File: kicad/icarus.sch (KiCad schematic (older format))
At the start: 78 parts, among them J1 CAN Bus, J2 CAN Bus, J3 SWD Programming, J4 USB_B_Micro, Q1 BSS123, U1 MAX15062A, U10 XT30, U11 XT30, U12 XT30, U13 XT30, U14 LT1787HVIMS8PBF, U15 USBLC6-2SC6, U16 STLM20DD9FUDFN-4L_STM-L, U2 STM32G474CEU6, U3 TCAN334G, U4 ZXMP10A13FTA, U5 XT90, U6 FSV10150VTO277-3L_ONS-L, U7 XT30, U8 XT30, U9 TPS2490DGSR

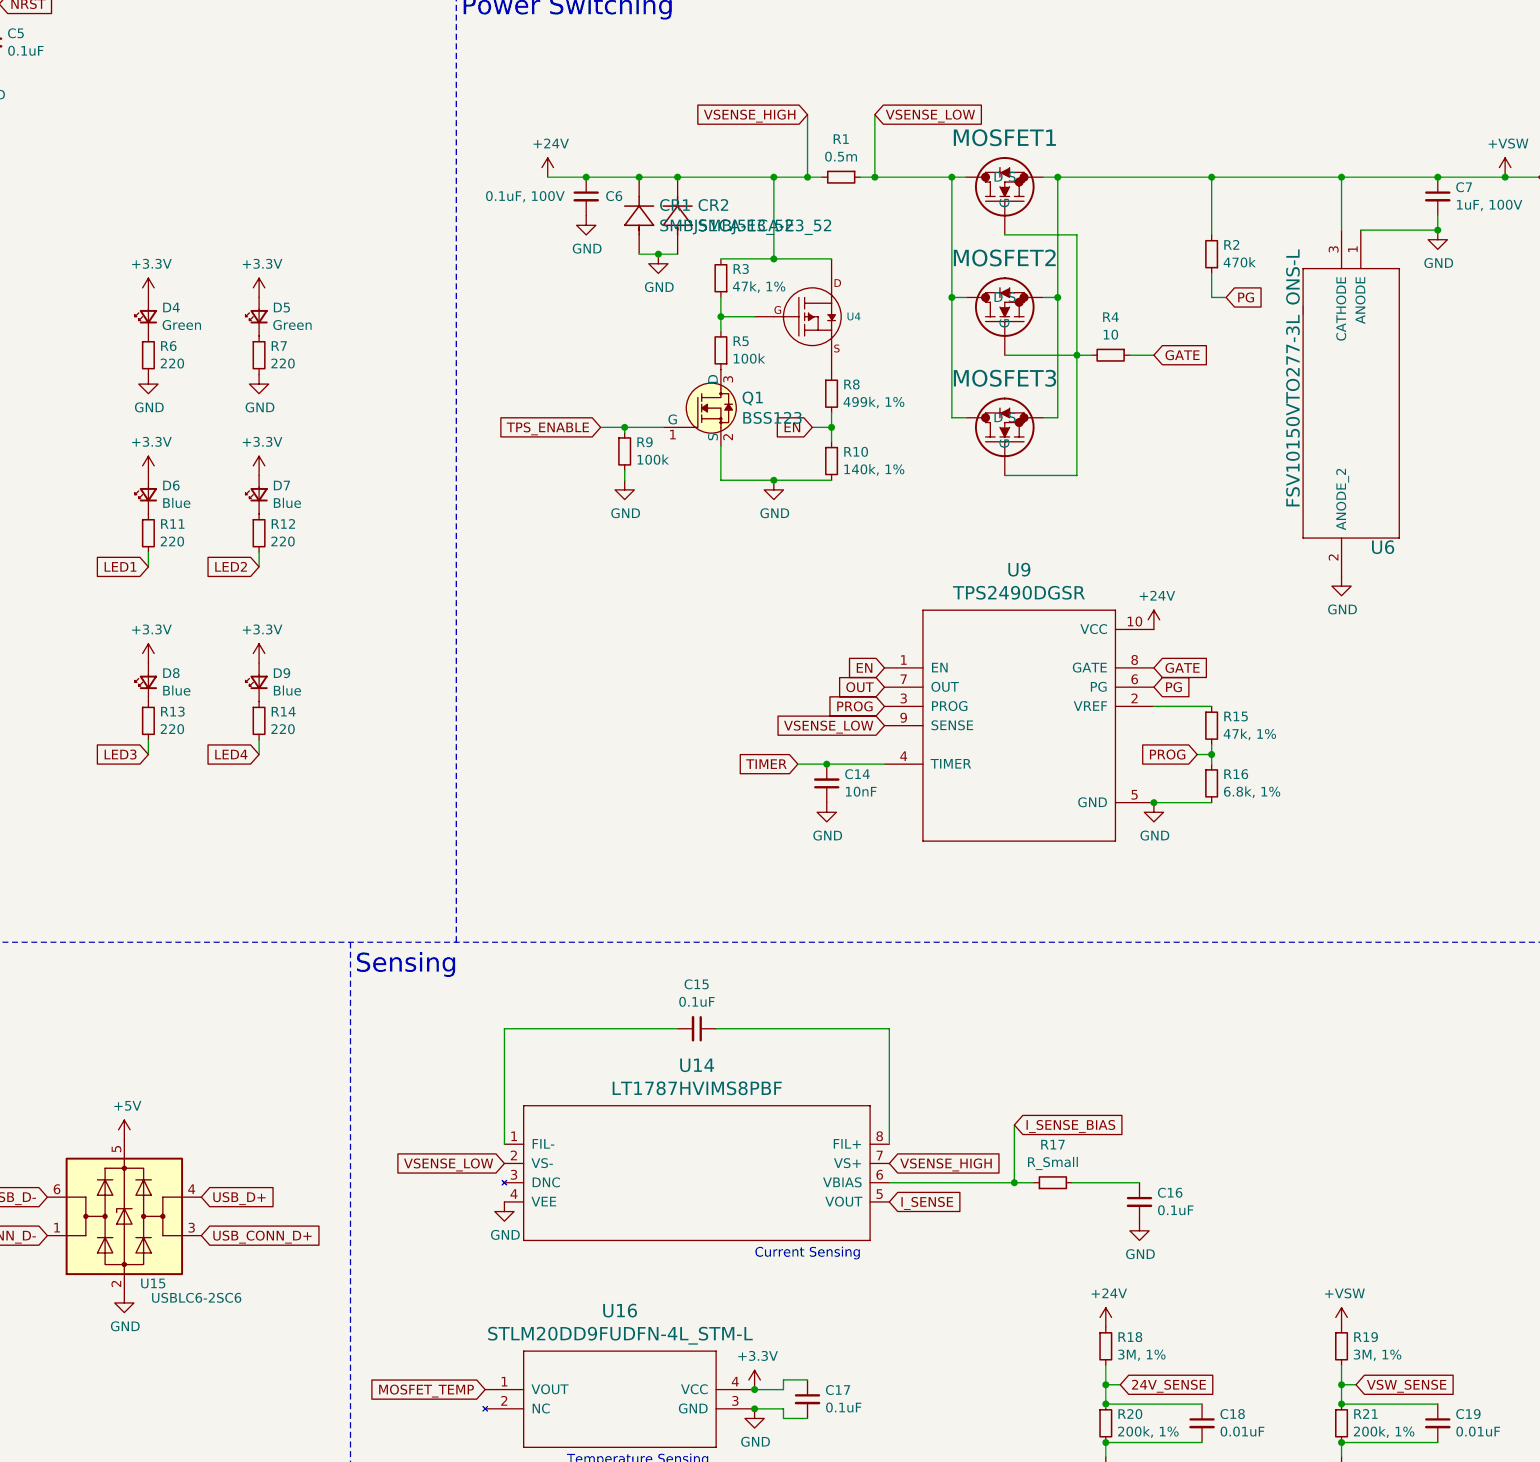
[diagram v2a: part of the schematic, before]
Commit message: Finished importing and modifying footprints
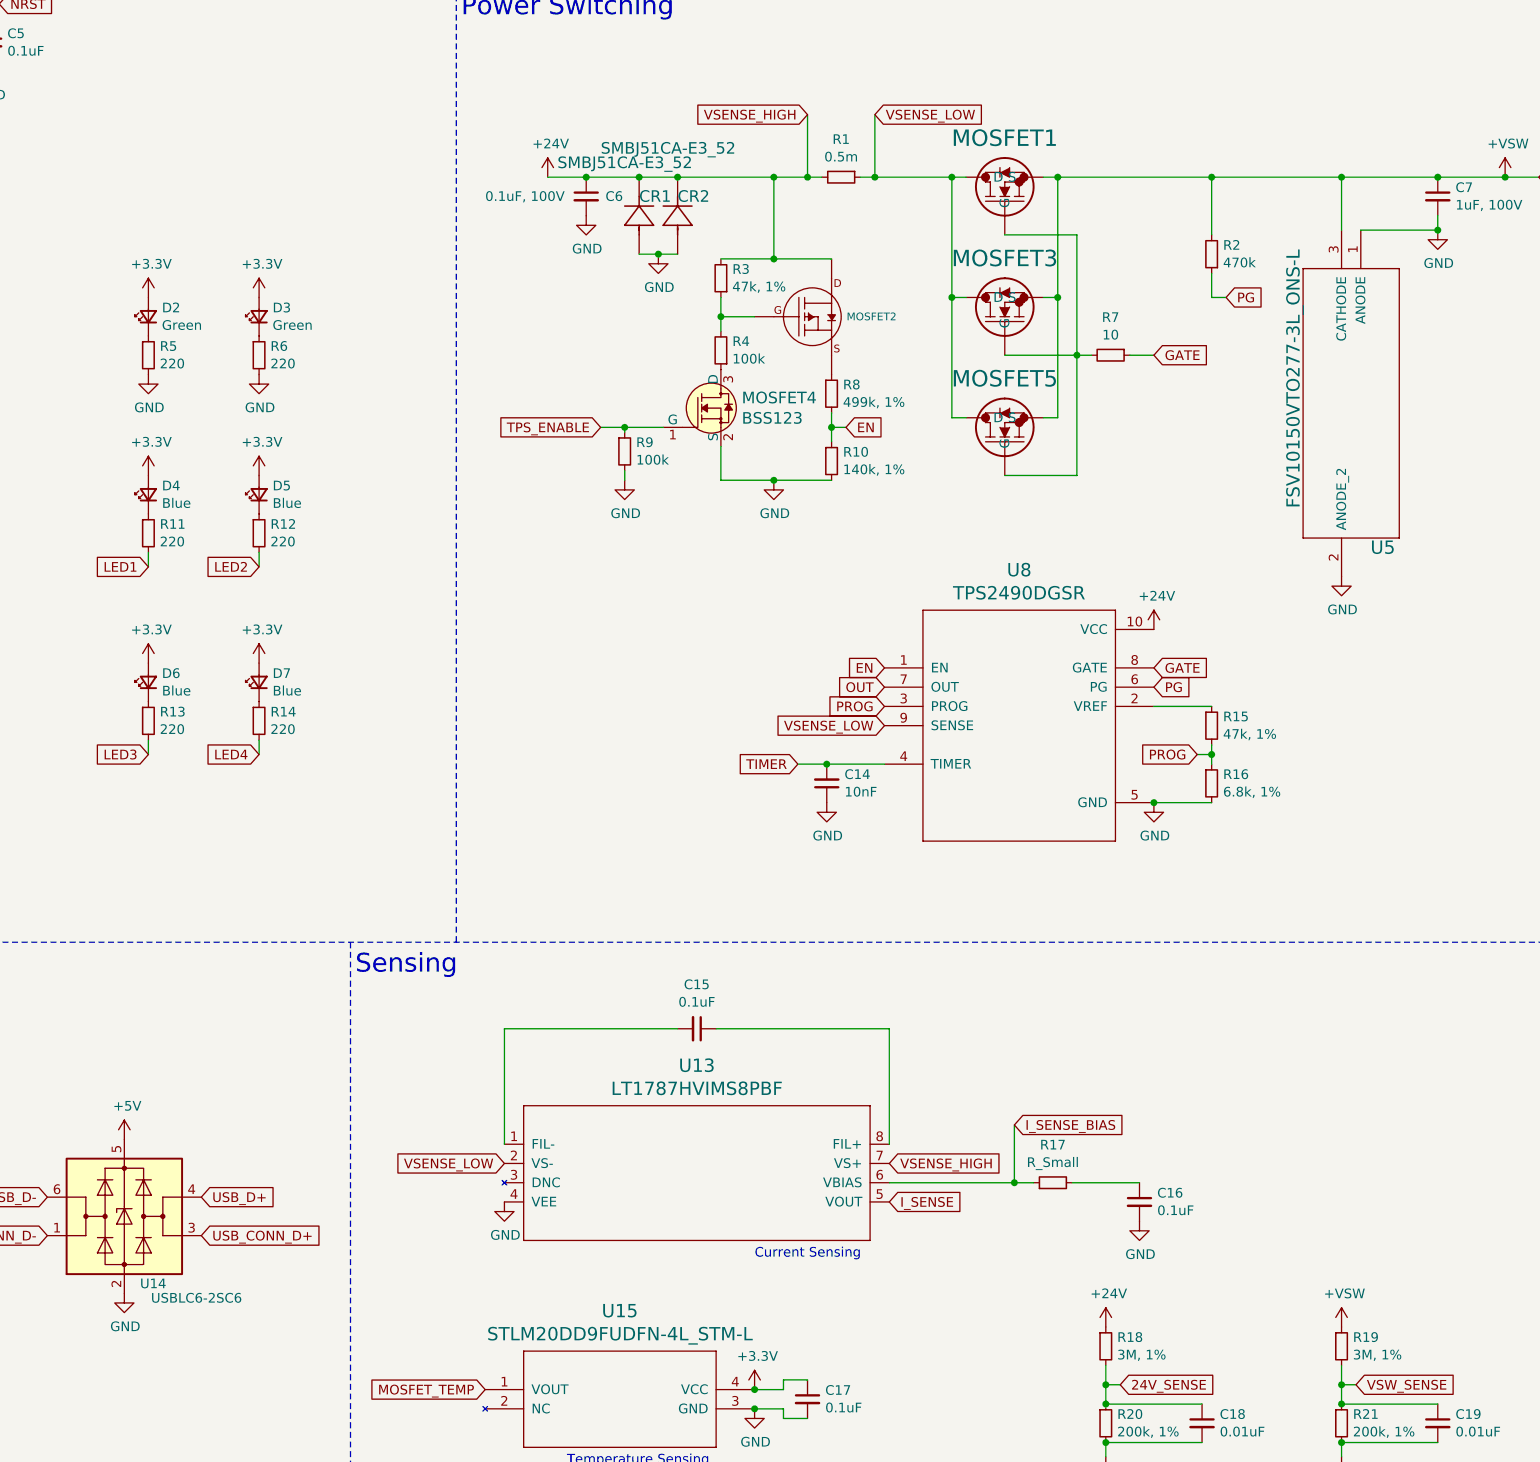
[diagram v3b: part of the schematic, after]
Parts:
- MOSFET2: renamed from U4; footprint digikey-footprints:SOT-23-3 -> icarus_kicad_lib:ZXMP10A13FTA
- renumbered D4 to D2, D5 to D3, D6 to D4, D7 to D5, D8 to D6, D9 to D7, MOSFET2 to MOSFET3, Q1 to MOSFET4, MOSFET3 to MOSFET5, R5 to R4, R6 to R5, R7 to R6, R4 to R7, U11 to U10, U12 to U11, U13 to U12, U14 to U13, U15 to U14, U16 to U15, U5 to U4, U6 to U5, U7 to U6, U8 to U7, U9 to U8, U10 to U9
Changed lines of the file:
@@
 $EndComp
 $Comp
-L Power_Protection:USBLC6-2SC6 U15
+L Power_Protection:USBLC6-2SC6 U14
 U 1 1 60480FBC
 P 4800 8925
-F 0 "U15" H 4950 8575 50  0000 C CNN
+F 0 "U14" H 4950 8575 50  0000 C CNN
 F 1 "USBLC6-2SC6" H 5175 8500 50  0000 C CNN
 F 2 "digikey-footprints:SOT-23-6" H 4800 8425 50  0001 C CNN
@@
 	13175 6475 13175 6600
 $Comp
-L xt30:XT30 U7
+L xt30:XT30 U6
 U 1 1 604E38EC
 P 15275 5700
-F 0 "U7" H 15325 5750 50  0001 C CNN
+F 0 "U6" H 15325 5750 50  0001 C CNN
 F 1 "XT30" H 15275 5700 50  0001 C CNN
 F 2 "icarus_kicad_lib:XT30P" H 15275 5700 50  0001 C CNN
@@
 $EndComp
 $Comp
-L xt30:XT30 U8
+L xt30:XT30 U7
 U 1 1 604E3CF6
 P 15275 6250
-F 0 "U8" H 15325 6300 50  0001 C CNN
+F 0 "U7" H 15325 6300 50  0001 C CNN
 F 1 "XT30" H 15275 6250 50  0001 C CNN
 F 2 "icarus_kicad_lib:XT30P" H 15275 6250 50  0001 C CNN
@@
 $EndComp
 $Comp
-L xt30:XT30 U10
+L xt30:XT30 U9
 U 1 1 604E3E54
 P 15275 6800
-F 0 "U10" H 15325 6850 50  0001 C CNN
+F 0 "U9" H 15325 6850 50  0001 C CNN
 F 1 "XT30" H 15275 6800 50  0001 C CNN
 F 2 "icarus_kicad_lib:XT30P" H 15275 6800 50  0001 C CNN
@@
 $EndComp
 $Comp
-L xt30:XT30 U11
+L xt30:XT30 U10
 U 1 1 604E4ABF
 P 15275 7350
-F 0 "U11" H 15325 7400 50  0001 C CNN
+F 0 "U10" H 15325 7400 50  0001 C CNN
 F 1 "XT30" H 15275 7350 50  0001 C CNN
 F 2 "icarus_kicad_lib:XT30P" H 15275 7350 50  0001 C CNN
@@
 $EndComp
 $Comp
-L xt30:XT30 U12
+L xt30:XT30 U11
 U 1 1 604E507D
 P 15275 7900
-F 0 "U12" H 15325 7950 50  0001 C CNN
+F 0 "U11" H 15325 7950 50  0001 C CNN
 F 1 "XT30" H 15275 7900 50  0001 C CNN
 F 2 "icarus_kicad_lib:XT30P" H 15275 7900 50  0001 C CNN
@@
 $EndComp
 $Comp
-L xt30:XT30 U13
+L xt30:XT30 U12
 U 1 1 604E565A
 P 15275 8450
-F 0 "U13" H 15325 8500 50  0001 C CNN
+F 0 "U12" H 15325 8500 50  0001 C CNN
 F 1 "XT30" H 15275 8450 50  0001 C CNN
 F 2 "icarus_kicad_lib:XT30P" H 15275 8450 50  0001 C CNN
@@
 ICARUS
 $Comp
-L tps2490dgsr:TPS2490DGSR U9
+L tps2490dgsr:TPS2490DGSR U8
 U 1 1 60502360
 P 9450 6375
-F 0 "U9" H 9450 7183 69  0000 C CNN
+F 0 "U8" H 9450 7183 69  0000 C CNN
 F 1 "TPS2490DGSR" H 9450 7063 69  0000 C CNN
 F 2 "icarus_kicad_lib:TPS2490DGSR" H 9450 6375 50  0001 C CNN
@@
 $EndComp
 $Comp
-L Device:LED_Small D5
+L Device:LED_Small D3
 U 1 1 607A30EE
 P 5500 4250
-F 0 "D5" V 5546 4180 50  0000 R CNN
+F 0 "D3" V 5546 4180 50  0000 R CNN
 F 1 "Green" V 5455 4180 50  0000 R CNN
 F 2 "LED_SMD:LED_0603_1608Metric" V 5500 4250 50  0001 C CNN
@@
 $EndComp
 $Comp
-L Device:R_Small R7
+L Device:R_Small R6
 U 1 1 607A30F4
 P 5500 4450
-F 0 "R7" H 5559 4496 50  0000 L CNN
+F 0 "R6" H 5559 4496 50  0000 L CNN
 F 1 "220" H 5559 4405 50  0000 L CNN
 F 2 "Resistor_SMD:R_0402_1005Metric" H 5500 4450 50  0001 C CNN
@@
 $EndComp
 $Comp
-L Device:LED_Small D6
+L Device:LED_Small D4
 U 1 1 607B09D4
 P 4925 5175
-F 0 "D6" V 4971 5105 50  0000 R CNN
+F 0 "D4" V 4971 5105 50  0000 R CNN
 F 1 "Blue" V 4880 5105 50  0000 R CNN
 F 2 "LED_SMD:LED_0603_1608Metric" V 4925 5175 50  0001 C CNN
@@
 $EndComp
 $Comp
-L Device:LED_Small D4
+L Device:LED_Small D2
 U 1 1 607D3F96
 P 4925 4250
-F 0 "D4" V 4971 4180 50  0000 R CNN
+F 0 "D2" V 4971 4180 50  0000 R CNN
 F 1 "Green" V 4880 4180 50  0000 R CNN
 F 2 "LED_SMD:LED_0603_1608Metric" V 4925 4250 50  0001 C CNN
@@
 $EndComp
 $Comp
-L Device:R_Small R6
+L Device:R_Small R5
 U 1 1 607D3F9C
 P 4925 4450
-F 0 "R6" H 4984 4496 50  0000 L CNN
+F 0 "R5" H 4984 4496 50  0000 L CNN
 F 1 "220" H 4984 4405 50  0000 L CNN
 F 2 "Resistor_SMD:R_0402_1005Metric" H 4925 4450 50  0001 C CNN
@@
 $EndComp
 $Comp
-L Device:LED_Small D7
+L Device:LED_Small D5
 U 1 1 607DF041
 P 5500 5175
-F 0 "D7" V 5546 5105 50  0000 R CNN
+F 0 "D5" V 5546 5105 50  0000 R CNN
 F 1 "Blue" V 5455 5105 50  0000 R CNN
 F 2 "LED_SMD:LED_0603_1608Metric" V 5500 5175 50  0001 C CNN
@@
 Connection ~ 1250 5525
 $Comp
-L lt1787hvims8pbf:LT1787HVIMS8PBF U14
+L lt1787hvims8pbf:LT1787HVIMS8PBF U13
 U 1 1 608530FA
 P 6575 8550
-F 0 "U14" H 7775 8958 69  0000 C CNN
+F 0 "U13" H 7775 8958 69  0000 C CNN
 F 1 "LT1787HVIMS8PBF" H 7775 8838 69  0000 C CNN
 F 2 "icarus_kicad_lib:LT1787HVIMS8PBF" H 6575 8550 50  0001 C CNN
@@
 $EndComp
 $Comp
-L xt30:XT30 U5
+L xt30:XT30 U4
 U 1 1 60883C89
 P 15275 4775
-F 0 "U5" H 15325 4825 50  0001 C CNN
+F 0 "U4" H 15325 4825 50  0001 C CNN
 F 1 "XT90" H 15275 4775 50  0001 C CNN
 F 2 "icarus_kicad_lib:XT90PW-M" H 15275 4775 50  0001 C CNN
@@
 Current Sensing
 $Comp
-L stlm20dd9fudfn-4l_stm-l:STLM20DD9FUDFN-4L_STM-L U16
+L stlm20dd9fudfn-4l_stm-l:STLM20DD9FUDFN-4L_STM-L U15
 U 1 1 60896628
 P 6575 9825
-F 0 "U16" H 7375 10233 69  0000 C CNN
+F 0 "U15" H 7375 10233 69  0000 C CNN
 F 1 "STLM20DD9FUDFN-4L_STM-L" H 7375 10113 69  0000 C CNN
 F 2 "icarus_kicad_lib:STLM20DD9FUDFN-4L_STM-L" H 6575 9825 50  0001 C CNN
@@
 	11625 3525 11975 3525
 $Comp
-L fsv10150vto277-3l_ons-l:FSV10150VTO277-3L_ONS-L U6
+L fsv10150vto277-3l_ons-l:FSV10150VTO277-3L_ONS-L U5
 U 1 1 60A04254
 P 11125 5700
-F 0 "U6" V 11375 5550 69  0000 R CNN
+F 0 "U5" V 11375 5550 69  0000 R CNN
 F 1 "FSV10150VTO277-3L_ONS-L" H 12925 5950 69  0000 R CNN
 F 2 "icarus_kicad_lib:FSV10150VTO277-3L_ONS-L" H 11125 5700 50  0001 C CNN
@@
 	1    0    0    -1
 $EndComp
-Text GLabel 8375 4825 0    50   Input ~ 0
+Text GLabel 8550 4825 2    50   Input ~ 0
 EN
-Wire Wire Line
-	8375 4825 8475 4825
-Wire Wire Line
-	8475 4750 8475 4825
-Connection ~ 8475 4825
-Wire Wire Line
-	8475 4825 8475 4900
 Text GLabel 8700 3200 2    50   Input ~ 0
 VSENSE_LOW
@@
 GATE
 $Comp
-L Device:R_Small R4
+L Device:R_Small R7
 U 1 1 605F126E
 P 9925 4450
-F 0 "R4" V 9729 4450 50  0000 C CNN
+F 0 "R7" V 9729 4450 50  0000 C CNN
 F 1 "10" V 9820 4450 50  0000 C CNN
 F 2 "Resistor_SMD:R_0402_1005Metric" H 9925 4450 50  0001 C CNN
@@
 $EndComp
 $Comp
-L p-channel_fet_sot-23-3:P-CHANNEL_FET_SOT-23-3 U4
+L p-channel_fet_sot-23-3:P-CHANNEL_FET_SOT-23-3 MOSFET2
 U 1 1 60BF3EC6
 P 8375 4250
-F 0 "U4" H 8553 4250 40  0000 L CNN
+F 0 "MOSFET2" H 8553 4250 40  0000 L CNN
 F 1 "ZXMP10A13FTA" H 8553 4212 40  0001 L CNN
-F 2 "digikey-footprints:SOT-23-3" H 8375 4250 50  0001 C CNN
+F 2 "icarus_kicad_lib:ZXMP10A13FTA" H 8375 4250 50  0001 C CNN
 F 3 "" H 8375 4250 50  0001 C CNN
 	1    8375 4250
@@
 $EndComp
 $Comp
-L Device:R_Small R5
+L Device:R_Small R4
 U 1 1 60BF6AD0
 P 7900 4425
-F 0 "R5" H 7841 4379 50  0000 R CNN
+F 0 "R4" H 7841 4379 50  0000 R CNN
 F 1 "100k" H 7841 4470 50  0000 R CNN
 F 2 "Resistor_SMD:R_0402_1005Metric" H 7900 4425 50  0001 C CNN
@@
 Connection ~ 3225 6750
 $Comp
-L Device:LED_Small D8
+L Device:LED_Small D6
 U 1 1 604C7C67
 P 4925 6150
-F 0 "D8" V 4971 6080 50  0000 R CNN
+F 0 "D6" V 4971 6080 50  0000 R CNN
 F 1 "Blue" V 4880 6080 50  0000 R CNN
 F 2 "LED_SMD:LED_0603_1608Metric" V 4925 6150 50  0001 C CNN
@@
 LED3
 $Comp
-L Device:LED_Small D9
+L Device:LED_Small D7
 U 1 1 604C7C7B
 P 5500 6150
-F 0 "D9" V 5546 6080 50  0000 R CNN
+F 0 "D7" V 5546 6080 50  0000 R CNN
 F 1 "Blue" V 5455 6080 50  0000 R CNN
 F 2 "LED_SMD:LED_0603_1608Metric" V 5500 6150 50  0001 C CNN
@@
 $EndComp
 $Comp
-L icarus-rescue:PSMN4R8-100BSEJ-psmn4r8-100bsej MOSFET2
+L icarus-rescue:PSMN4R8-100BSEJ-psmn4r8-100bsej MOSFET3
 U 1 1 6088724D
 P 9375 4450
-F 0 "MOSFET2" V 9877 4450 85  0000 C CNN
+F 0 "MOSFET3" V 9877 4450 85  0000 C CNN
 F 1 "PSMN4R8-100BSEJ" V 9877 4450 85  0001 C CNN
 F 2 "icarus_kicad_lib:PSMN4R8-100BSEJ" H 9375 4450 50  0001 C CNN
@@
 $EndComp
 $Comp
-L icarus-rescue:PSMN4R8-100BSEJ-psmn4r8-100bsej MOSFET3
+L icarus-rescue:PSMN4R8-100BSEJ-psmn4r8-100bsej MOSFET5
 U 1 1 60888AB1
 P 9375 5075
-F 0 "MOSFET3" V 9877 5075 85  0000 C CNN
+F 0 "MOSFET5" V 9877 5075 85  0000 C CNN
 F 1 "PSMN4R8-100BSEJ" V 9877 5075 85  0001 C CNN
 F 2 "icarus_kicad_lib:PSMN4R8-100BSEJ" H 9375 5075 50  0001 C CNN
@@
 U 1 1 608E4AFE
 P 7475 3925
-F 0 "CR1" V 7728 3821 60  0000 R CNN
-F 1 "SMBJ51CA-E3_52" V 7622 3821 60  0000 R CNN
+F 0 "CR1" V 7775 3925 60  0000 R CNN
+F 1 "SMBJ51CA-E3_52" V 7950 4350 60  0000 R CNN
 F 2 "icarus_kicad_lib:SMBJ51CA-E3-52" H 7675 3565 60  0001 C CNN
 F 3 "" H 7475 3925 60  0000 C CNN
@@
 U 1 1 608F0D36
 P 7675 3925
-F 0 "CR2" V 7928 3821 60  0000 R CNN
-F 1 "SMBJ51CA-E3_52" V 7822 3821 60  0000 R CNN
+F 0 "CR2" V 7975 3925 60  0000 R CNN
+F 1 "SMBJ51CA-E3_52" V 8225 4325 60  0000 R CNN
 F 2 "icarus_kicad_lib:SMBJ51CA-E3-52" H 7875 3565 60  0001 C CNN
 F 3 "" H 7675 3925 60  0000 C CNN
@@
 	7575 3925 7675 3925
 $Comp
-L dk_Transistors-FETs-MOSFETs-Single:BSS123 Q1
+L dk_Transistors-FETs-MOSFETs-Single:BSS123 MOSFET4
 U 1 1 60925E78
 P 7900 4725
-F 0 "Q1" H 8008 4778 60  0000 L CNN
+F 0 "MOSFET4" H 8008 4778 60  0000 L CNN
 F 1 "BSS123" H 8008 4672 60  0000 L CNN
 F 2 "digikey-footprints:SOT-23-3" H 8100 4925 60  0001 L CNN
@@
 	0    1    1    0
 $EndComp
+Wire Wire Line
+	8475 4750 8475 4825
+Wire Wire Line
+	8550 4825 8475 4825
+Connection ~ 8475 4825
+Wire Wire Line
+	8475 4825 8475 4900
 $EndSCHEMATC

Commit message: Initial rough layout done
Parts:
- J1, J2: footprint Connector_JST:JST_PH_B3B-PH-SM4-TB_1x03-1MP_P2.00mm_Vertical -> Connector_JST:JST_PH_B3B-PH-K_1x03_P2.00mm_Vertical
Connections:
- net GND: now also C10.2, C11.2, C12.2, C13.2, C8.2, C9.2
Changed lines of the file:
@@
 F 0 "J1" H 14055 3342 50  0000 L CNN
 F 1 "CAN Bus" H 14055 3251 50  0000 L CNN
-F 2 "Connector_JST:JST_PH_B3B-PH-SM4-TB_1x03-1MP_P2.00mm_Vertical" H 13975 3300 50  0001 C CNN
+F 2 "Connector_JST:JST_PH_B3B-PH-K_1x03_P2.00mm_Vertical" H 13975 3300 50  0001 C CNN
 F 3 "~" H 13975 3300 50  0001 C CNN
 	1    13975 3300
@@
 F 0 "J2" H 15230 3342 50  0000 L CNN
 F 1 "CAN Bus" H 15230 3251 50  0000 L CNN
-F 2 "Connector_JST:JST_PH_B3B-PH-SM4-TB_1x03-1MP_P2.00mm_Vertical" H 15150 3300 50  0001 C CNN
+F 2 "Connector_JST:JST_PH_B3B-PH-K_1x03_P2.00mm_Vertical" H 15150 3300 50  0001 C CNN
 F 3 "~" H 15150 3300 50  0001 C CNN
 	1    15150 3300
@@
 Wire Wire Line
 	8475 4825 8475 4900
+$Comp
+L power:GND #PWR?
+U 1 1 60A47D8A
+P 1225 6825
+F 0 "#PWR?" H 1225 6575 50  0001 C CNN
+F 1 "GND" H 1230 6652 50  0000 C CNN
+F 2 "" H 1225 6825 50  0001 C CNN
+F 3 "" H 1225 6825 50  0001 C CNN
+	1    1225 6825
+	1    0    0    -1
+$EndComp
 $EndSCHEMATC

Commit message: Compressed board layout, about to start traces
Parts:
- R1: footprint Resistor_SMD:R_0402_1005Metric -> Resistor_SMD:R_2512_6332Metric
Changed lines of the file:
@@
 F 0 "R1" V 8329 3525 50  0000 C CNN
 F 1 "0.5m" V 8420 3525 50  0000 C CNN
-F 2 "Resistor_SMD:R_0402_1005Metric" H 8525 3525 50  0001 C CNN
+F 2 "Resistor_SMD:R_2512_6332Metric" H 8525 3525 50  0001 C CNN
 F 3 "~" H 8525 3525 50  0001 C CNN
 	1    8525 3525
@@
 	8475 4825 8475 4900
 $Comp
-L power:GND #PWR?
+L power:GND #PWR0157
 U 1 1 60A47D8A
 P 1225 6825
-F 0 "#PWR?" H 1225 6575 50  0001 C CNN
+F 0 "#PWR0157" H 1225 6575 50  0001 C CNN
 F 1 "GND" H 1230 6652 50  0000 C CNN
 F 2 "" H 1225 6825 50  0001 C CNN
